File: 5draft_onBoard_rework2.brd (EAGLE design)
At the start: 100 x 82.5 mm, 69 parts, among them IC3 74ABT125PW, IC4 MAX4466KS, J2 USB_MINI-B_DIGIKEY, Q1 NPN 40V 1A SOT-23

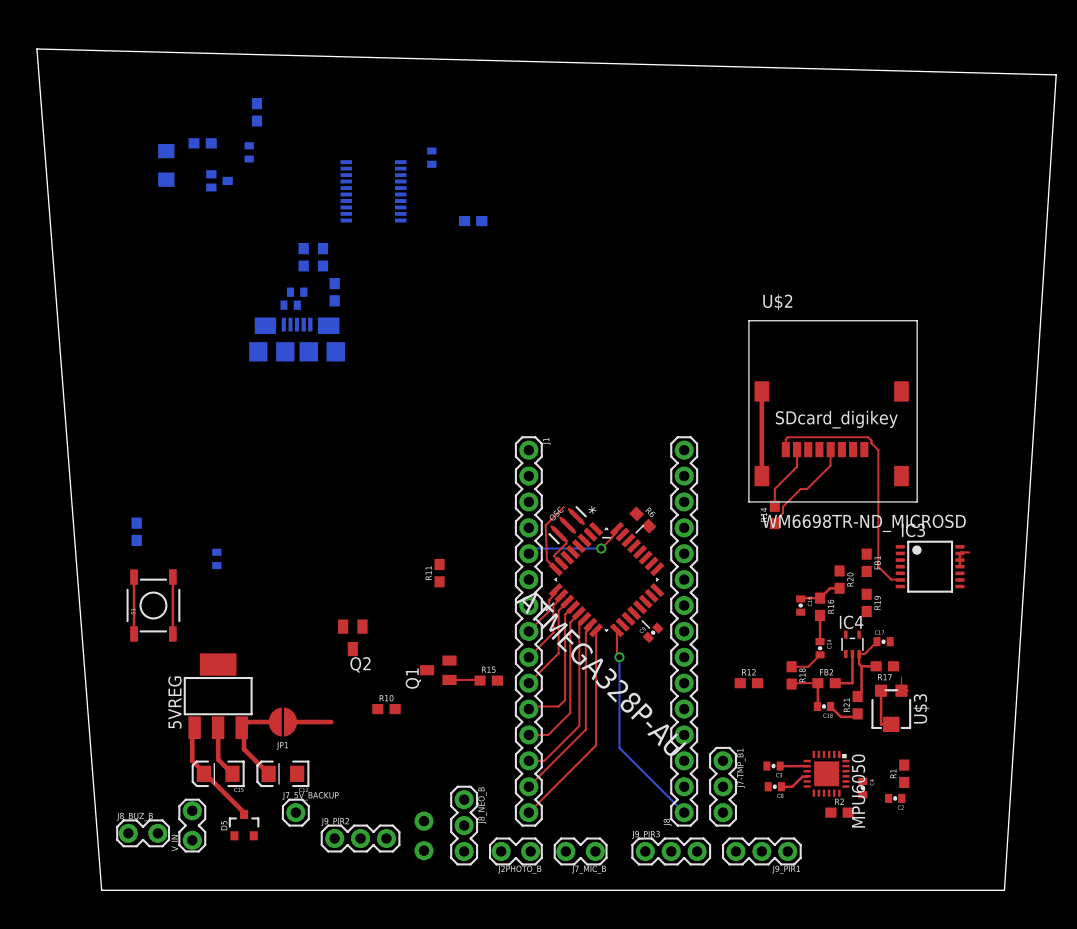
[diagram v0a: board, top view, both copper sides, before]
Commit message: redoing layout, condensing.
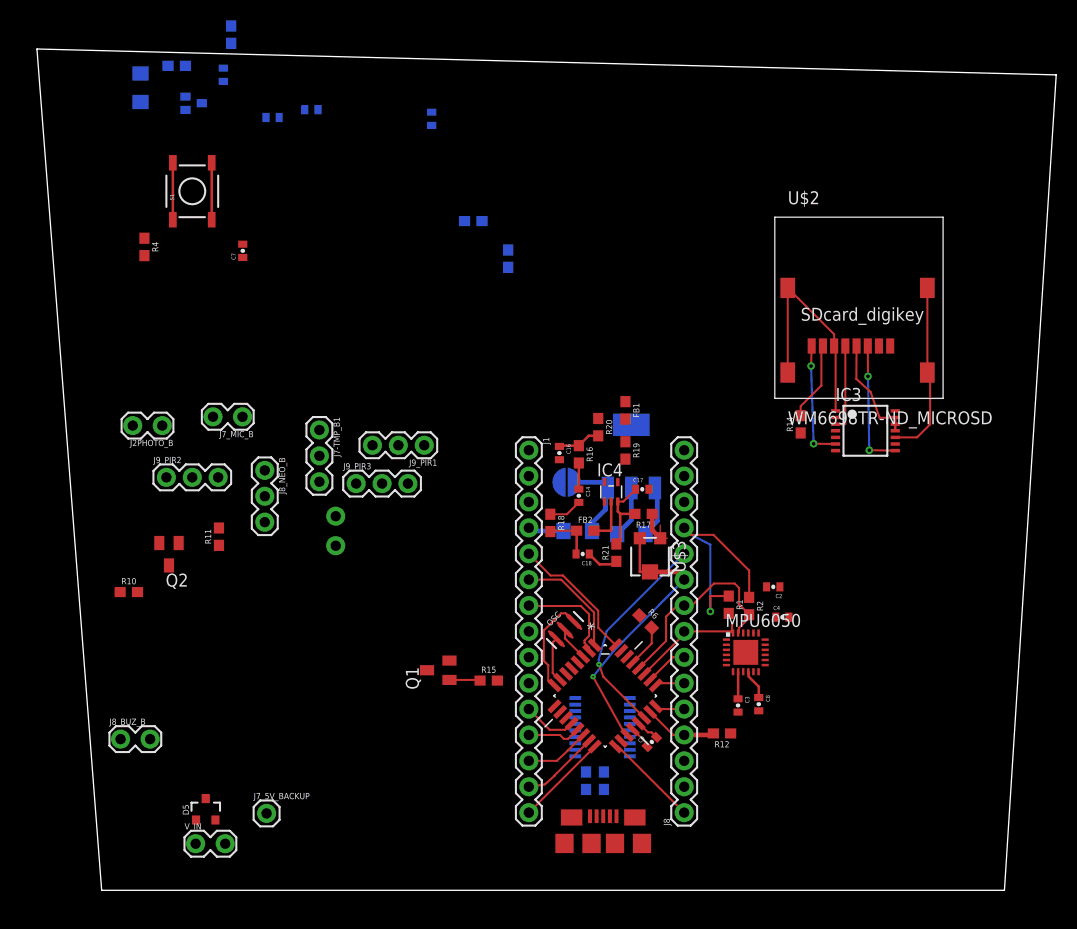
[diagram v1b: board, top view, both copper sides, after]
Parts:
- moved R7 58.4 mm to (47.5, 6.93)
- moved R5 58.3 mm to (49.3, 6.93)
- moved FTDI231XS1 57.2 mm to (49.1, 12.2)
- moved J2 56.8 mm to (49.2, 0.79), flipped to the top
- moved J2PHOTO_B 55.2 mm to (5.77, 41.8)
- moved J7_MIC_B 54.9 mm to (13.6, 42.6)
- moved J9_PIR1 53.5 mm to (31.6, 39.9)
- moved J7-TMP_B1 51.2 mm to (21.4, 41.4)
- moved 5VREG 46.9 mm to (52.0, 38.8), flipped to the bottom
- moved C15 46.9 mm to (52.0, 31.1), flipped to the bottom
- moved J9_PIR3 45.9 mm to (25.0, 36.1)
- moved S1 40.8 mm to (8.89, 64.8)
- moved J9_PIR2 39.1 mm to (6.35, 36.7)
- moved J8_NEO_B 37.8 mm to (16.0, 37.4)
- moved C12 37.5 mm to (46.7, 31.4), flipped to the bottom
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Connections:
- net D+_P renamed DN+_P
- net D-_N renamed DN_N
- net N$10 renamed DAT1
- net USBDM_N renamed USBD_M
- net USBDM_P renamed USBD_P
- net SCL: now also ATMEGA328P-AU.28; no longer ATMEGA328P-AU.27
- net SDA: now also ATMEGA328P-AU.27; no longer ATMEGA328P-AU.28
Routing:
- net GND: track 28.5 -> 69.1 mm
- net A6: track 4.30 -> 27.8 mm, vias 0 -> 1
- net A7: track 0.00 -> 21.1 mm, vias 0 -> 1
- net SCL: track 0.00 -> 20.1 mm
- net 5V: track 15.6 -> 34.3 mm, vias 0 -> 1
- net DAT1: track 25.0 -> 11.7 mm, vias 0 -> 2
- net SS_BUFF: track 0.00 -> 12.8 mm, vias 0 -> 2
- net SDA: track 0.00 -> 11.7 mm
- net SCK: track 20.6 -> 9.41 mm, vias 1 -> 0
- net D3: track 0.18 -> 11.0 mm
- net SS: track 17.1 -> 6.37 mm
- net MOSI: track 18.4 -> 7.69 mm
- net D4: track 0.00 -> 10.2 mm
- net MISO: track 27.1 -> 16.9 mm
- net D9: track 15.1 -> 5.32 mm
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
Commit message: need to add sensors next
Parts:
- moved U$1 80.0 mm to (54.5, 7.62)
- moved R3 76.3 mm to (54.6, 17.1), turned to 180 degrees
- moved C6 73.6 mm to (51.8, 6.10), turned to 180 degrees
- moved R8 71.9 mm to (45.7, 16.3), turned to 180 degrees
- moved C10 71.8 mm to (45.5, 6.22)
- moved C11 71.6 mm to (37.8, 11.9), turned to 90 degrees
- moved C5 69.4 mm to (39.9, 12.7), turned to 270 degrees
- moved C1 61.6 mm to (54.7, 14.5), turned to 90 degrees
- moved FB3 45.7 mm to (44.5, 12.7)
- moved R9 44.9 mm to (54.2, 20.6), turned to 45 degrees
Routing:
- net VUSB: track 0.00 -> 33.7 mm, vias 0 -> 2
- net GND: track 69.1 -> 96.5 mm, vias 0 -> 1
- net 3.3VFTDI: track 0.00 -> 18.3 mm
- net RX: track 0.00 -> 9.06 mm
- net RX-I: track 0.00 -> 7.02 mm, vias 0 -> 1
- net DN+_P: track 0.00 -> 4.64 mm, vias 0 -> 1
- net DN_N: track 0.06 -> 4.54 mm, vias 0 -> 1
- net TX-O: track 0.00 -> 3.04 mm, vias 0 -> 1
- net DTR_FTDI: track 0.00 -> 2.98 mm
- net TX: track 0.00 -> 2.10 mm
- net 5V: track 34.3 -> 35.3 mm, vias 1 -> 2

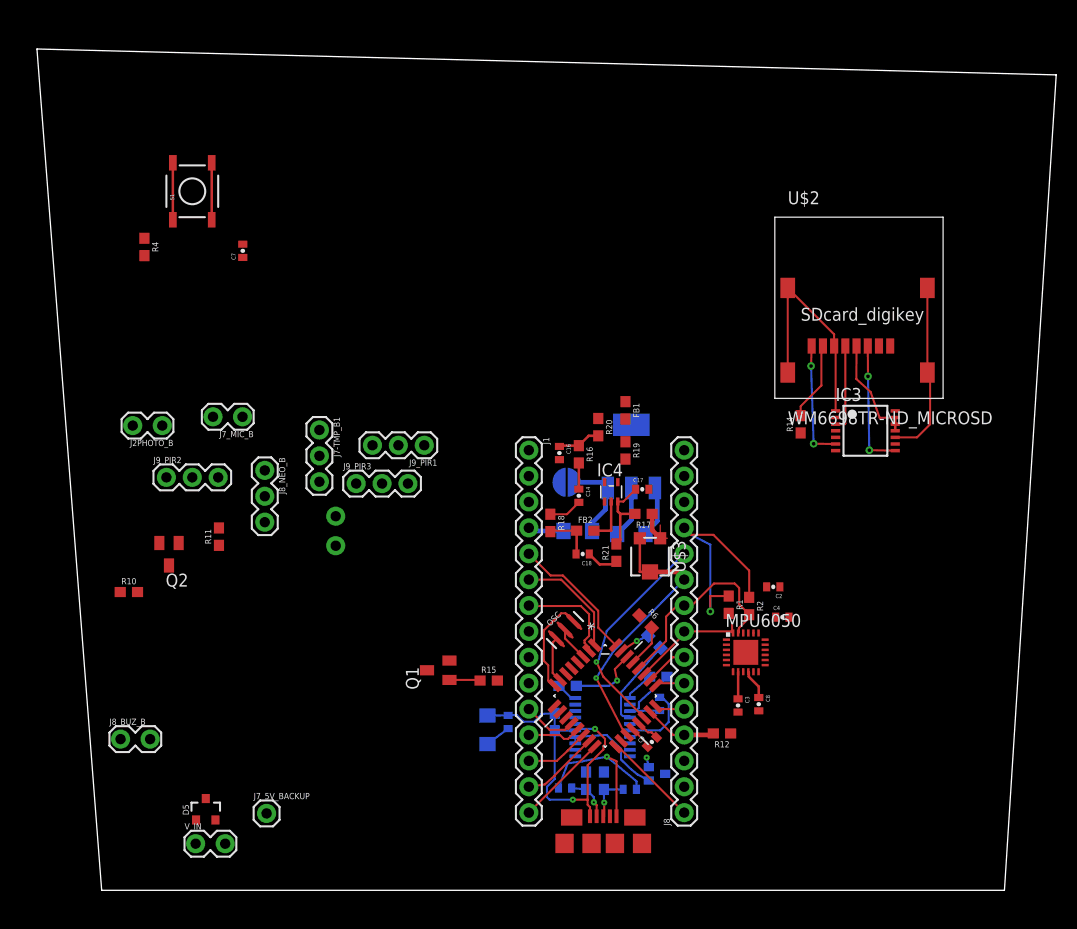
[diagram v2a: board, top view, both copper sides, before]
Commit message: 3rd draft, close to final. FTDI might need to be reworked. and there is a bug. I do not know why AVCC is routed to VCC when it should not be, cannot find net causing issue
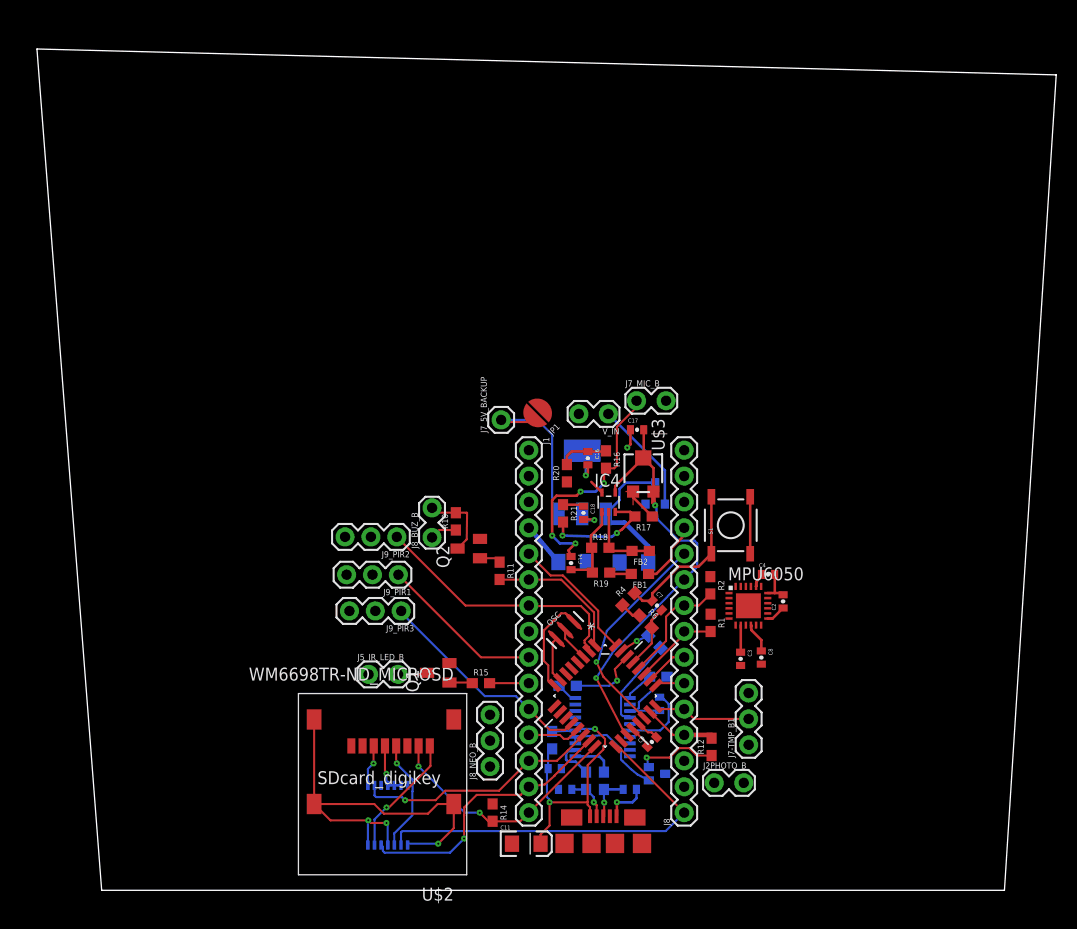
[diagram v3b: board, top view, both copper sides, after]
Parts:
- moved J2PHOTO_B 64.8 mm to (60.3, 6.73), turned to 0 degrees
- moved S1 62.2 mm to (61.7, 32.0)
- moved IC3 60.2 mm to (28.1, 3.56), flipped to the bottom, turned to 0 degrees
- moved R4 58.7 mm to (51.7, 24.8), turned to 45 degrees
- moved V_IN 58.2 mm to (49.5, 42.9), turned to 180 degrees
- moved D5 53.9 mm to (54.3, 35.1), flipped to the bottom
- moved C7 53.5 mm to (54.5, 24.1), turned to 315 degrees
- moved J7-TMP_B1 52.2 mm to (63.5, 10.5), turned to 90 degrees
- moved R14 48.6 mm to (38.4, 3.81), turned to 270 degrees
- moved U$2 47.2 mm to (34.5, 13.0), turned to 180 degrees
- moved J7_5V_BACKUP 44.9 mm to (39.2, 42.3), turned to 90 degrees
- moved J7_MIC_B 39.0 mm to (52.7, 44.2), turned to 0 degrees
- moved J8_NEO_B 36.5 mm to (38.1, 8.33), turned to 90 degrees
- moved J8_BUZ_B 36.4 mm to (32.4, 31.0), turned to 90 degrees
- moved R10 32.8 mm to (34.7, 32.4), turned to 90 degrees
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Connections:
- net N$17 renamed MICNET1K
- net N$24 renamed MIC_IN_C14
- net N$25 renamed MIC_IN+
- net D6: now also J9_PIR1.1
- net D7: no longer J9_PIR1.1
- net GND: now also J2.SHIELD, J2.SHIELD1, J2.SHIELD2, J2.SHIELD3, J2.SHIELD4, J2.SHIELD5
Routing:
- net SCK: track 9.41 -> 39.2 mm
- net MIC_IN_C14: track 2.60 -> 23.4 mm, vias 0 -> 4
- net MOSI: track 7.69 -> 27.2 mm, vias 0 -> 1
- net SS: track 6.37 -> 24.7 mm, vias 0 -> 1
- net D8: track 5.30 -> 23.0 mm
- net D6: track 0.00 -> 16.2 mm
- net D4: track 10.2 -> 26.0 mm
- net A6: track 27.4 -> 42.2 mm, vias 1 -> 2
- net 5V: track 35.3 -> 24.1 mm
- net N$22: track 0.06 -> 11.1 mm
- net DTR: track 5.59 -> 15.8 mm
- net VIN: track 5.09 -> 14.4 mm
- net GND: track 96.5 -> 87.6 mm, vias 1 -> 6
- net SS_BUFF: track 12.8 -> 4.11 mm, vias 2 -> 1
- net 5REGOUT: track 7.86 -> 16.4 mm
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
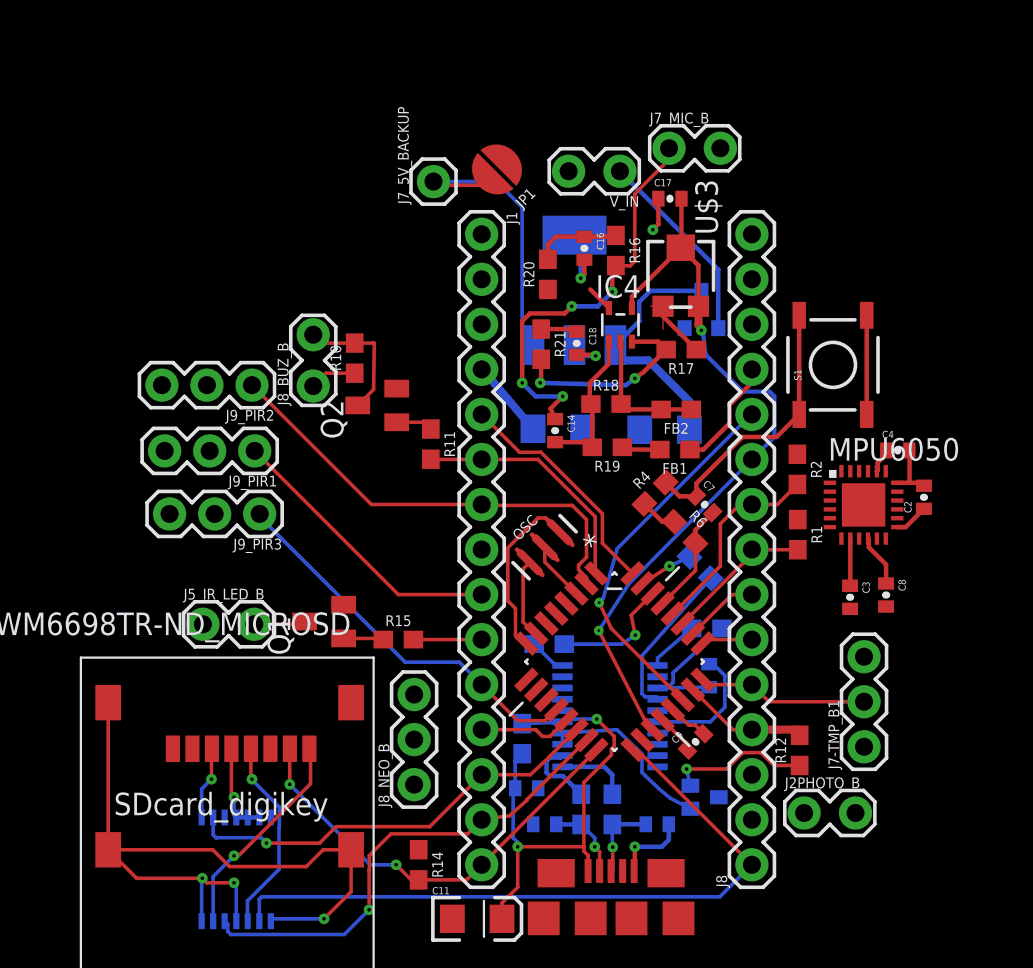
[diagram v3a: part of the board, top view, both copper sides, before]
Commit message: Rx, TX, and FTDI 3.3v traces are very difficult to route at this time. Also need to do ground planes
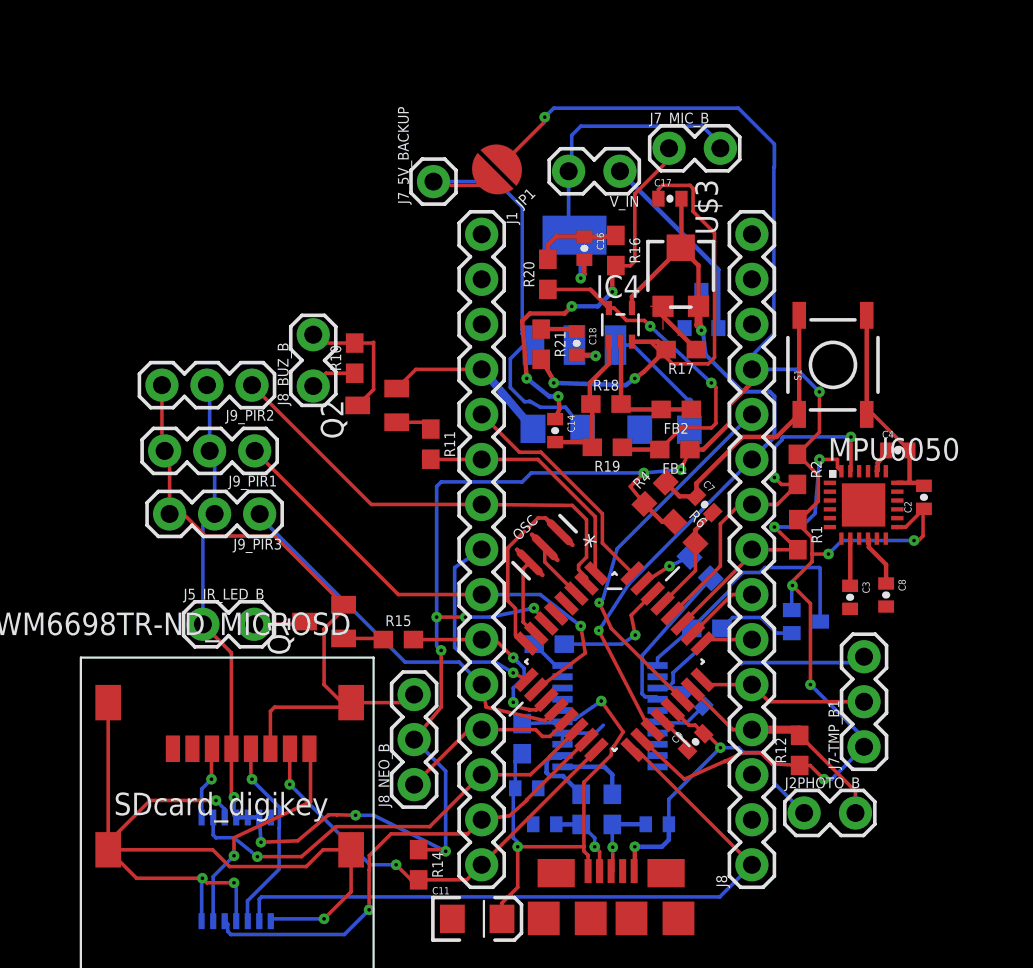
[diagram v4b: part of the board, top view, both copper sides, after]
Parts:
- moved U$1 11.4 mm to (60.2, 17.5)
- moved C1 1.48 mm to (54.0, 13.2), turned to 225 degrees
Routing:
- net 5V: track 24.1 -> 181.7 mm, vias 2 -> 17
- net GND: track 87.6 -> 173.5 mm, vias 6 -> 8
- net AVCC: track 3.64 -> 19.7 mm, vias 0 -> 2
- net N$30: track 13.2 -> 28.8 mm, vias 3 -> 2
- net DTR_FTDI: track 2.98 -> 14.8 mm
- net D6: track 16.2 -> 27.4 mm, vias 0 -> 1
- net D5: track 0.00 -> 11.0 mm, vias 0 -> 1
- net SCL: track 12.2 -> 21.9 mm, vias 0 -> 2
- net SDA: track 8.38 -> 17.7 mm, vias 0 -> 2
- net 5REGOUT: track 16.4 -> 24.8 mm
- net D7: track 3.85 -> 11.8 mm, vias 0 -> 2
- net VIN: track 14.4 -> 7.97 mm
- net A0: track 7.29 -> 13.0 mm
- net D9: track 5.32 -> 10.4 mm
- net 3.3VFTDI: track 18.3 -> 14.7 mm
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
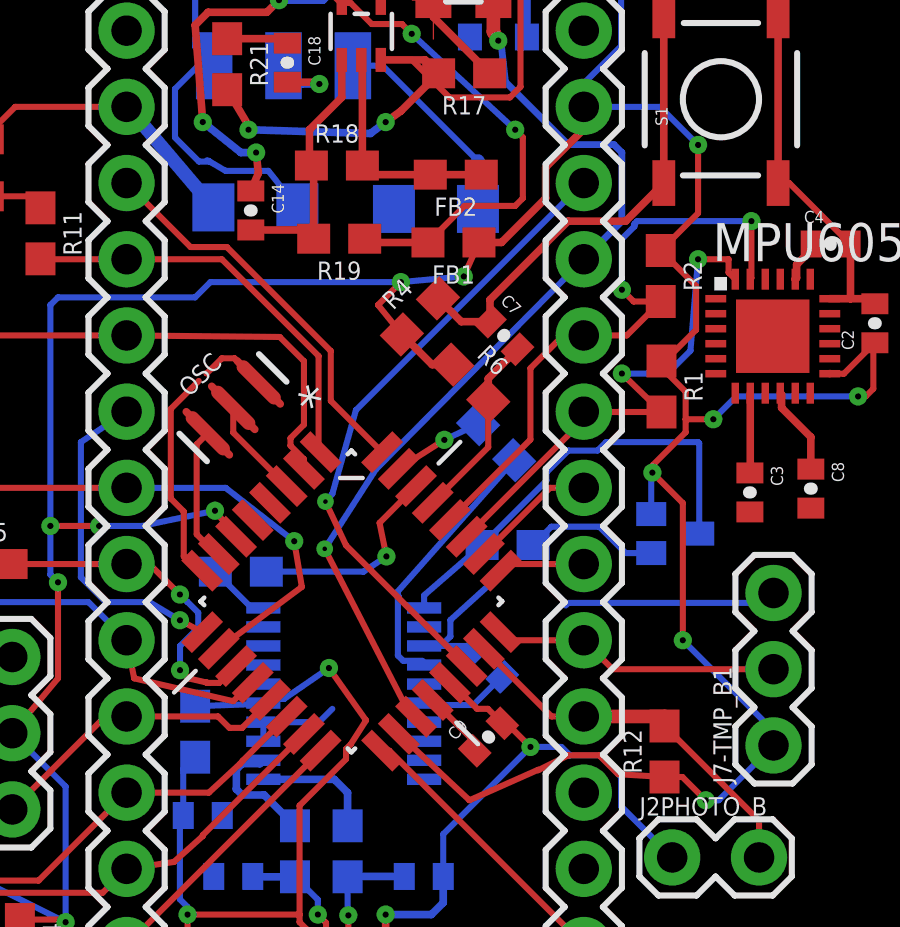
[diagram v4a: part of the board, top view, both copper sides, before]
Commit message: Ground planes should be the last thing, and doulbe check the RX Tx of FTDI to processor
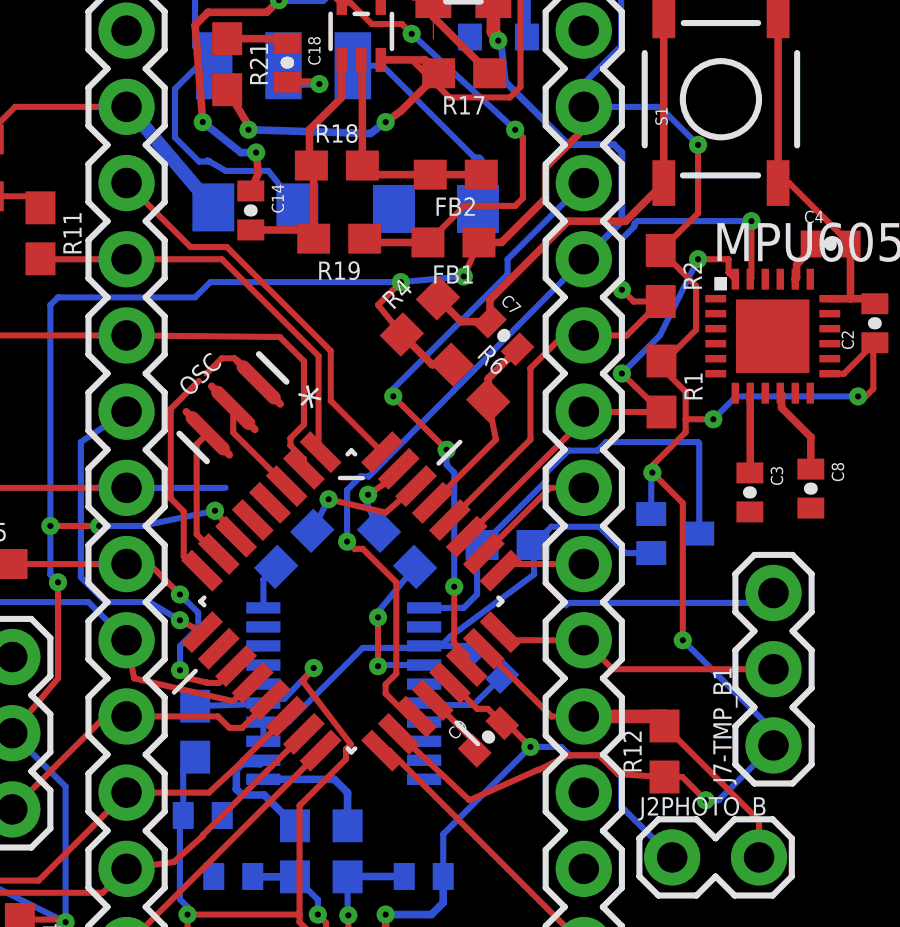
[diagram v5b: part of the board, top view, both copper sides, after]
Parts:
- moved R9 4.85 mm to (50.9, 17.0)
- moved R8 1.93 mm to (47.5, 17.0), turned to 135 degrees
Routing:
- net D6: track 27.4 -> 19.5 mm, vias 1 -> 0
- net 3.3VFTDI: track 14.7 -> 18.8 mm
- net RX: track 8.92 -> 5.29 mm, vias 0 -> 2
- net RX-I: track 7.02 -> 4.48 mm
- net A7: track 21.3 -> 19.8 mm, vias 1 -> 3
- net SDA: track 17.7 -> 16.6 mm
- net A6: track 42.2 -> 43.1 mm
- net DTR_FTDI: track 14.8 -> 15.5 mm
